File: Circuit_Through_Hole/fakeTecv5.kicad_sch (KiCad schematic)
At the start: 33 parts, among them J1 EXTRA, J12 FET2 3,3, J14 GPS Pins, J16 Encoder Pads, J2 Conn_01x04_Socket, J3 FET2 Drain, J38 JST-SH-4, J4 FET2 3,3, J46 Conn_01x02_Socket, J5 I2C Oled screen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

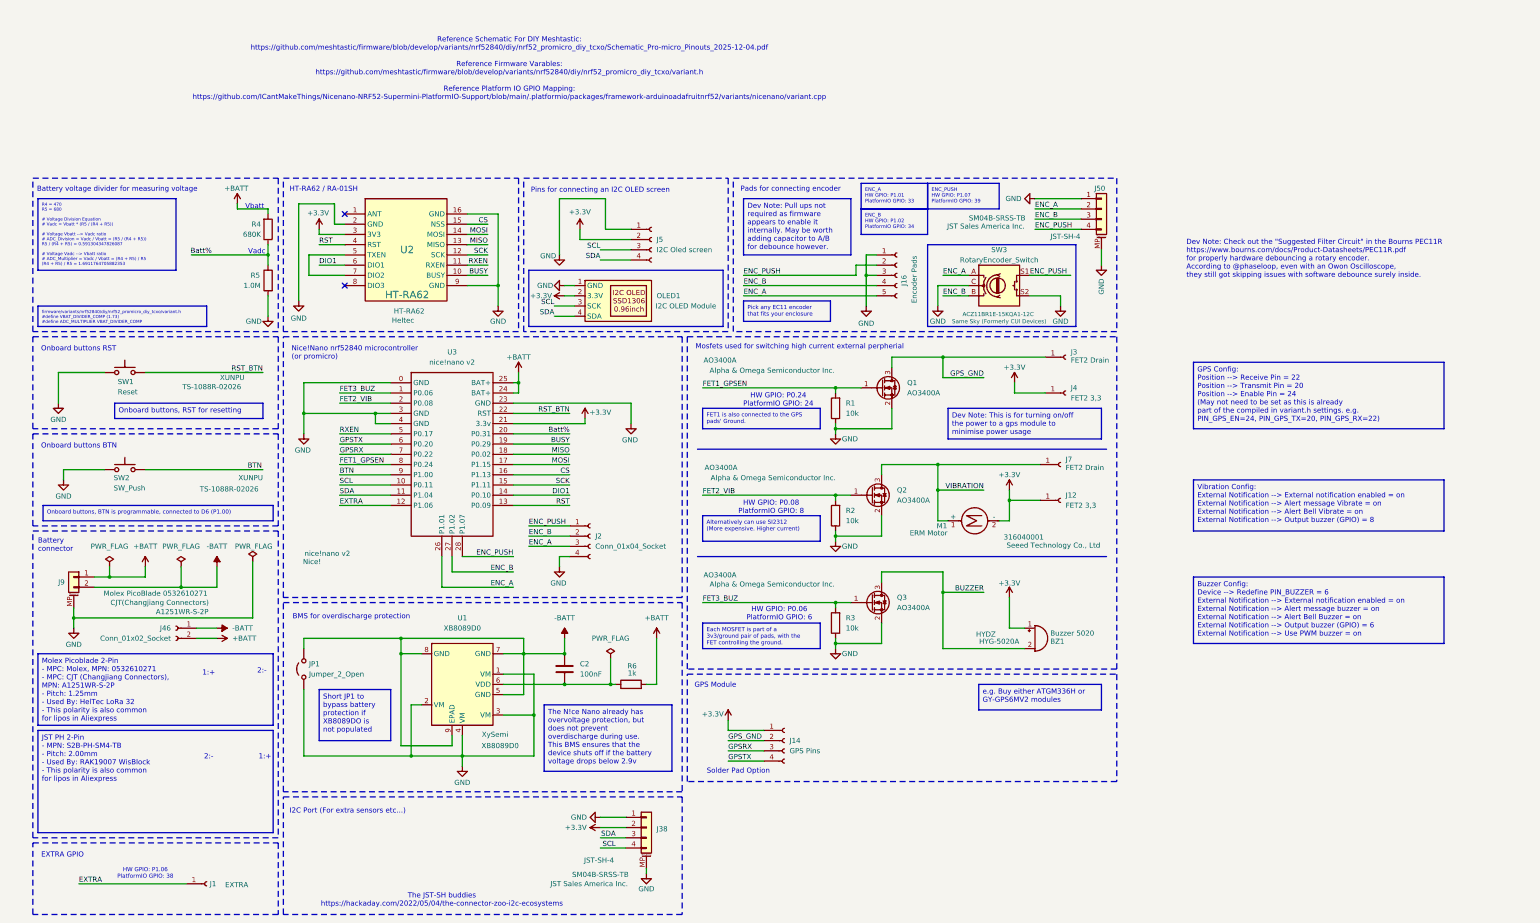
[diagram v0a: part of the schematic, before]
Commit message: sch: add more dev notes to explain why DIO1 and DIO2 is connected the way they were
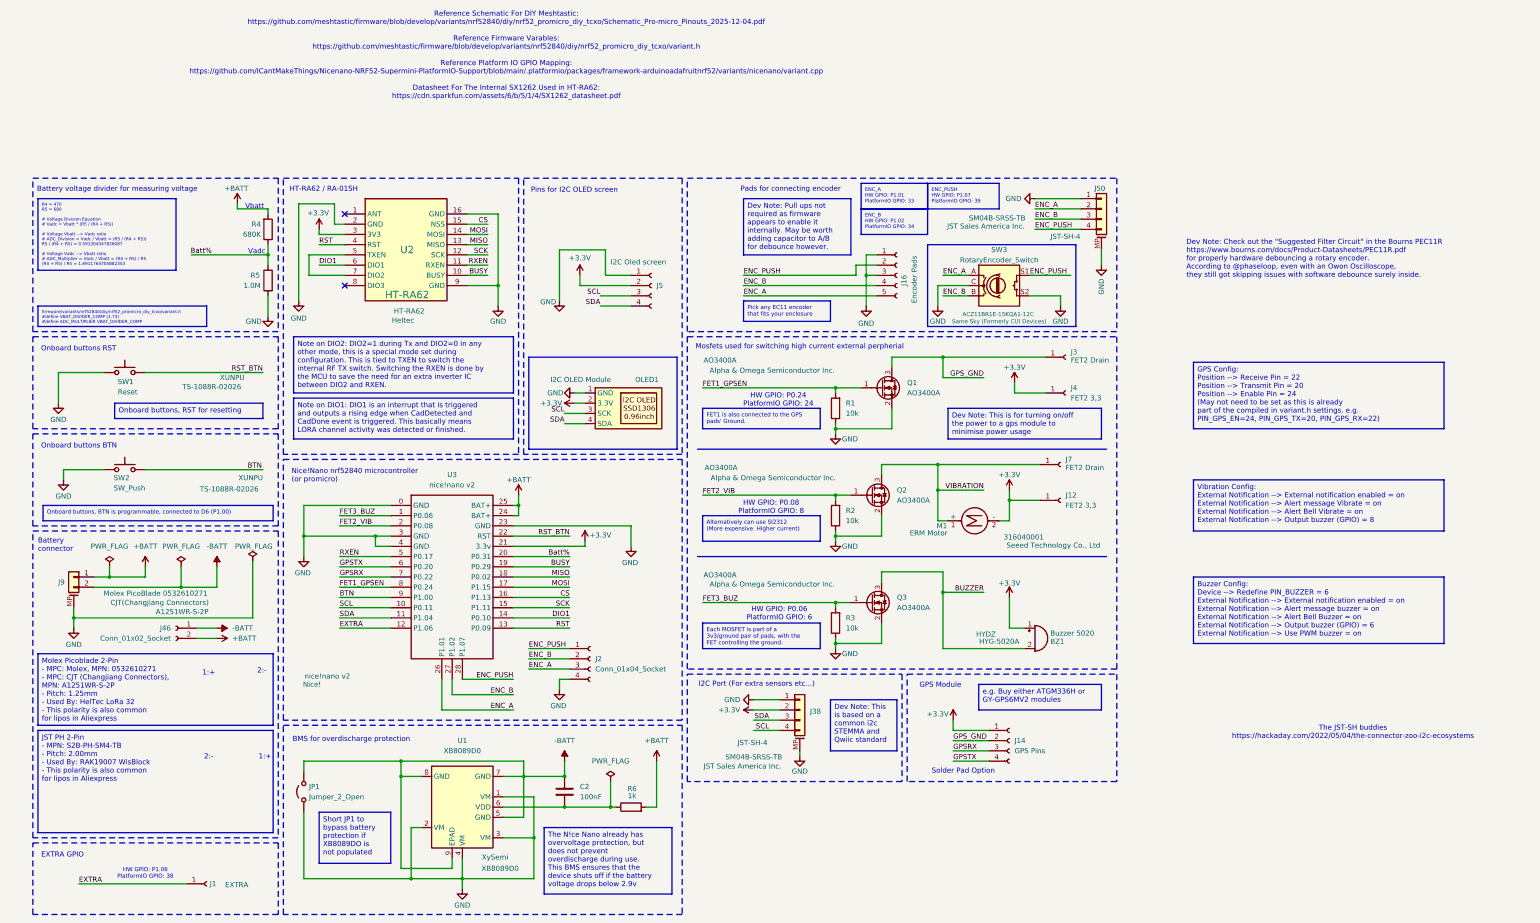
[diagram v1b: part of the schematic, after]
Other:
- note added: "Pins for I2C OLED screen"
- note removed: "Pins for connecting an I2C OLED screen"
- moved on the sheet: C2, J14, J2, J38, J5, JP1, OLED1, R6, U1, U3
